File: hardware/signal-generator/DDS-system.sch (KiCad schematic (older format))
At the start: 17 parts

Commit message: [Signal Generator] Layout microcontroller and allocate its pins
The microcontroller is the brains of the function generator system - it
is responsible for controlling the DDS signal generator system, as well
as the LCD module which provides the user interface. The specific
microcontroller used in this project is the ATmega2561-16AU from the
megaAVR uC family. The reasons I have picked this particular part are
the following:
- I am familiar with the AVR uC structure;
- it provides more SRAM memory (8 kB) than other MCUs of the same family;
- it has fewer pins (and therefore peripherals) than the ATmega2560.
Only a fraction of the available peripheral pins of the ATmega2561 have
been utilized in the current design. The remaining port pins (which are
internally connected to useful peripherals such as JTAG, XMEM, etc.)
are connected to pin header connectors and are meant for
upgrading/modifying the system as a whole by including additional
external circuitry. The ATmega2561's SPI port is also connected to a
similar pin header connector which allows the uC to play the role of an
SPI slave device.
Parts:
- removed U?: AD9764AR, Housings_SOIC:SOIC-28W_7.5x17.9mm_Pitch1.27mm, symbol TxDAC:AD9764AR
- removed U?: CY7C1021D-10ZSXI, symbol SRAMs:CY7C1021D-10ZSXI
- removed U?: DS1085Z-10+, symbol Frequency_Synthesizers:DS1085Z-10+
- added U?: AD9764AR, Housings_SOIC:SOIC-28W_7.5x17.9mm_Pitch1.27mm, symbol ulib_TxDAC:AD9764AR
- added U?: CY7C1021D-10ZSXI, symbol ulib_SRAMs:CY7C1021D-10ZSXI
- added U?: DS1085Z-10+, symbol ulib_Frequency_Synthesizers:DS1085Z-10+
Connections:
- net labels added: IOExINTA, IOExINTB
- wire segments 175 -> 177
- no-connect marks 2 -> 0
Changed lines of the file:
@@
 $Descr A4 11693 8268
 encoding utf-8
-Sheet 2 4
+Sheet 2 6
 Title "Digital Function Generator v2 - DDS System"
-Date "2019-11-05"
+Date "2019-12-01"
 Rev "1"
 Comp "Petar Nikolov"
@@
 Comment4 ""
 $EndDescr
-$Comp
-L TxDAC:AD9764AR U?
-U 1 1 5DBB83CF
-P 8100 2500
-F 0 "U?" H 7650 1550 50  0000 C CNN
-F 1 "AD9764AR" H 8500 1550 50  0000 C CNN
-F 2 "Housings_SOIC:SOIC-28W_7.5x17.9mm_Pitch1.27mm" H 8100 2450 50  0001 C CNN
-F 3 "https://www.analog.com/media/en/technical-documentation/data-sheets/AD9764.pdf" H 8100 2550 50  0001 C CNN
-	1    8100 2500
-	1    0    0    -1
-$EndComp
-$Comp
-L SRAMs:CY7C1021D-10ZSXI U?
-U 1 1 5DBB84FF
-P 5250 2550
-F 0 "U?" H 4800 3750 50  0000 C CNN
-F 1 "CY7C1021D-10ZSXI" V 5250 2550 50  0000 C CNN
-F 2 "" H 4450 3300 50  0001 C CNN
-F 3 "https://www.cypress.com/file/42721/download" H 5250 2600 50  0001 C CNN
-	1    5250 2550
-	1    0    0    -1
-$EndComp
-$Comp
-L Frequency_Synthesizers:DS1085Z-10+ U?
-U 1 1 5DBB873B
-P 1550 3350
-F 0 "U?" H 1200 3050 50  0000 C CNN
-F 1 "DS1085Z-10+" H 1900 3050 50  0000 C CNN
-F 2 "" H 0   3300 50  0001 C CNN
-F 3 "https://datasheets.maximintegrated.com/en/ds/DS1085.pdf" H 1550 3350 50  0001 C CNN
-	1    1550 3350
-	1    0    0    -1
-$EndComp
 $Comp
 L Interface_Expansion:MCP23017_SO U?
@@
 Wire Wire Line
 	5250 6800 5250 6900
-NoConn ~ 4550 5500
-NoConn ~ 4550 5600
 Wire Wire Line
 	4550 6300 4450 6300
@@
 	1    0    0    -1
 $EndComp
+$Comp
+L ulib_TxDAC:AD9764AR U?
+U 1 1 5DDD4020
+P 8100 2500
+F 0 "U?" H 8550 1550 50  0000 C CNN
+F 1 "AD9764AR" H 7650 1550 50  0000 C CNN
+F 2 "Housings_SOIC:SOIC-28W_7.5x17.9mm_Pitch1.27mm" H 8100 2450 50  0001 C CNN
+F 3 "https://www.analog.com/media/en/technical-documentation/data-sheets/AD9764.pdf" H 8100 2550 50  0001 C CNN
+	1    8100 2500
+	1    0    0    -1
+$EndComp
+$Comp
+L ulib_SRAMs:CY7C1021D-10ZSXI U?
+U 1 1 5DDE4989
+P 5250 2550
+F 0 "U?" H 5800 1350 50  0000 C CNN
+F 1 "CY7C1021D-10ZSXI" V 5250 2600 50  0000 C CNN
+F 2 "" H 4450 3300 50  0001 C CNN
+F 3 "https://www.cypress.com/file/42721/download" H 5250 2600 50  0001 C CNN
+	1    5250 2550
+	1    0    0    -1
+$EndComp
+$Comp
+L ulib_Frequency_Synthesizers:DS1085Z-10+ U?
+U 1 1 5DDE50A7
+P 1550 3350
+F 0 "U?" H 1200 3050 50  0000 C CNN
+F 1 "DS1085Z-10+" H 1900 3050 50  0000 C CNN
+F 2 "" H 0   3300 50  0001 C CNN
+F 3 "https://datasheets.maximintegrated.com/en/ds/DS1085.pdf" H 1550 3350 50  0001 C CNN
+	1    1550 3350
+	1    0    0    -1
+$EndComp
+Wire Wire Line
+	4550 5500 4450 5500
+Wire Wire Line
+	4450 5600 4550 5600
+Text HLabel 4450 5600 0    50   Input ~ 0
+IOExINTA
+Text HLabel 4450 5500 0    50   Input ~ 0
+IOExINTB
 $EndSCHEMATC

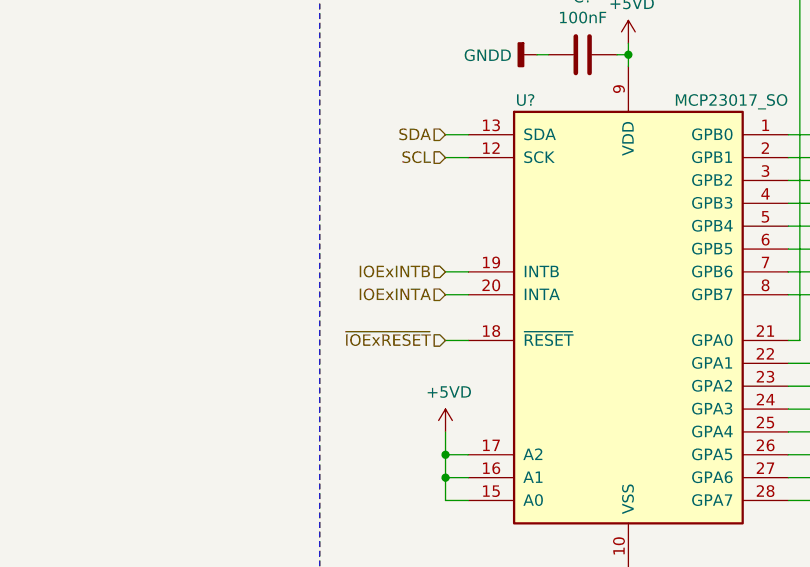
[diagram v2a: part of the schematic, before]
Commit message: [Signal Generator] Add DAC output conversion stage
The additional opamp stage is a differential amplifier configuration
which converts the differential current outputs of the DAC to a singular
voltage output in the range -0.5V to +0.5V.

The electrical schematic has overall been finalized with this addition.
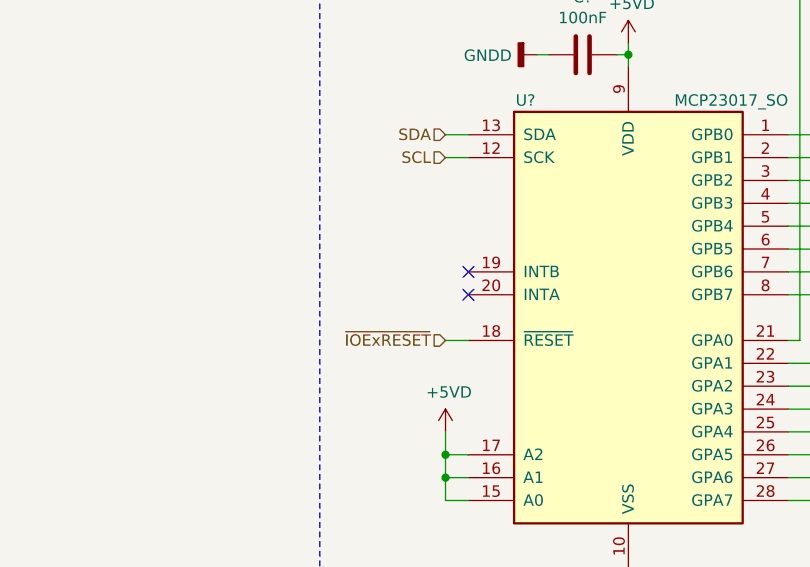
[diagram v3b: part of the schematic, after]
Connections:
- net IOExINTA: no longer names the net of U?.20 (INTA)
- net IOExINTB: no longer names the net of U?.19 (INTB)
- no-connect marks 0 -> 2
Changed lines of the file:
@@
 $Descr A4 11693 8268
 encoding utf-8
-Sheet 2 7
+Sheet 2 6
 Title "Digital Function Generator v2 - DDS System"
-Date "2019-12-01"
+Date "2019-12-08"
 Rev "1"
 Comp "Petar Nikolov"
@@
 	1    0    0    -1
 $EndComp
-Wire Wire Line
-	4550 5500 4450 5500
-Wire Wire Line
-	4450 5600 4550 5600
-Text HLabel 4450 5600 0    50   Input ~ 0
-IOExINTA
-Text HLabel 4450 5500 0    50   Input ~ 0
-IOExINTB
+NoConn ~ 4550 5600
+NoConn ~ 4550 5500
 $EndSCHEMATC

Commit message: [Signal Generator] Implement +3.3VD line with TC1017 voltage regulator
Up until now, the +3.3VD line was implemented using the L78L33 linear
voltage regulator. However, the latter has a dropout voltage of 2V which
means that the L78L33 cannot output a stable +3.3V from a +5V input.

To solve the aforementioned problem the TC1017 LDO voltage regulator has
replaced the L78L33. The former has a low dropout voltage of 180mV (typ.) at
100mA load current.
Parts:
- C? (x9): footprint (none) -> Capacitors_SMD:C_1206_HandSoldering
- C? (x2): footprint (none) -> Capacitors_Tantalum_SMD:CP_Tantalum_Case-A_EIA-3216-18_Hand
- R?: footprint (none) -> Resistors_SMD:R_1206_HandSoldering
- U?: footprint Package_SO:SOIC-28W_7.5x17.9mm_P1.27mm -> Housings_SOIC:SOIC-28W_7.5x17.9mm_Pitch1.27mm
- U?: footprint (none) -> Housings_SOIC:SOIC-14_3.9x8.7mm_Pitch1.27mm
- U?: footprint (none) -> SOP80P1176X120-44N:SOP80P1176X120-44N
- U?: footprint (none) -> Housings_SOIC:SOIC-8_3.9x4.9mm_Pitch1.27mm

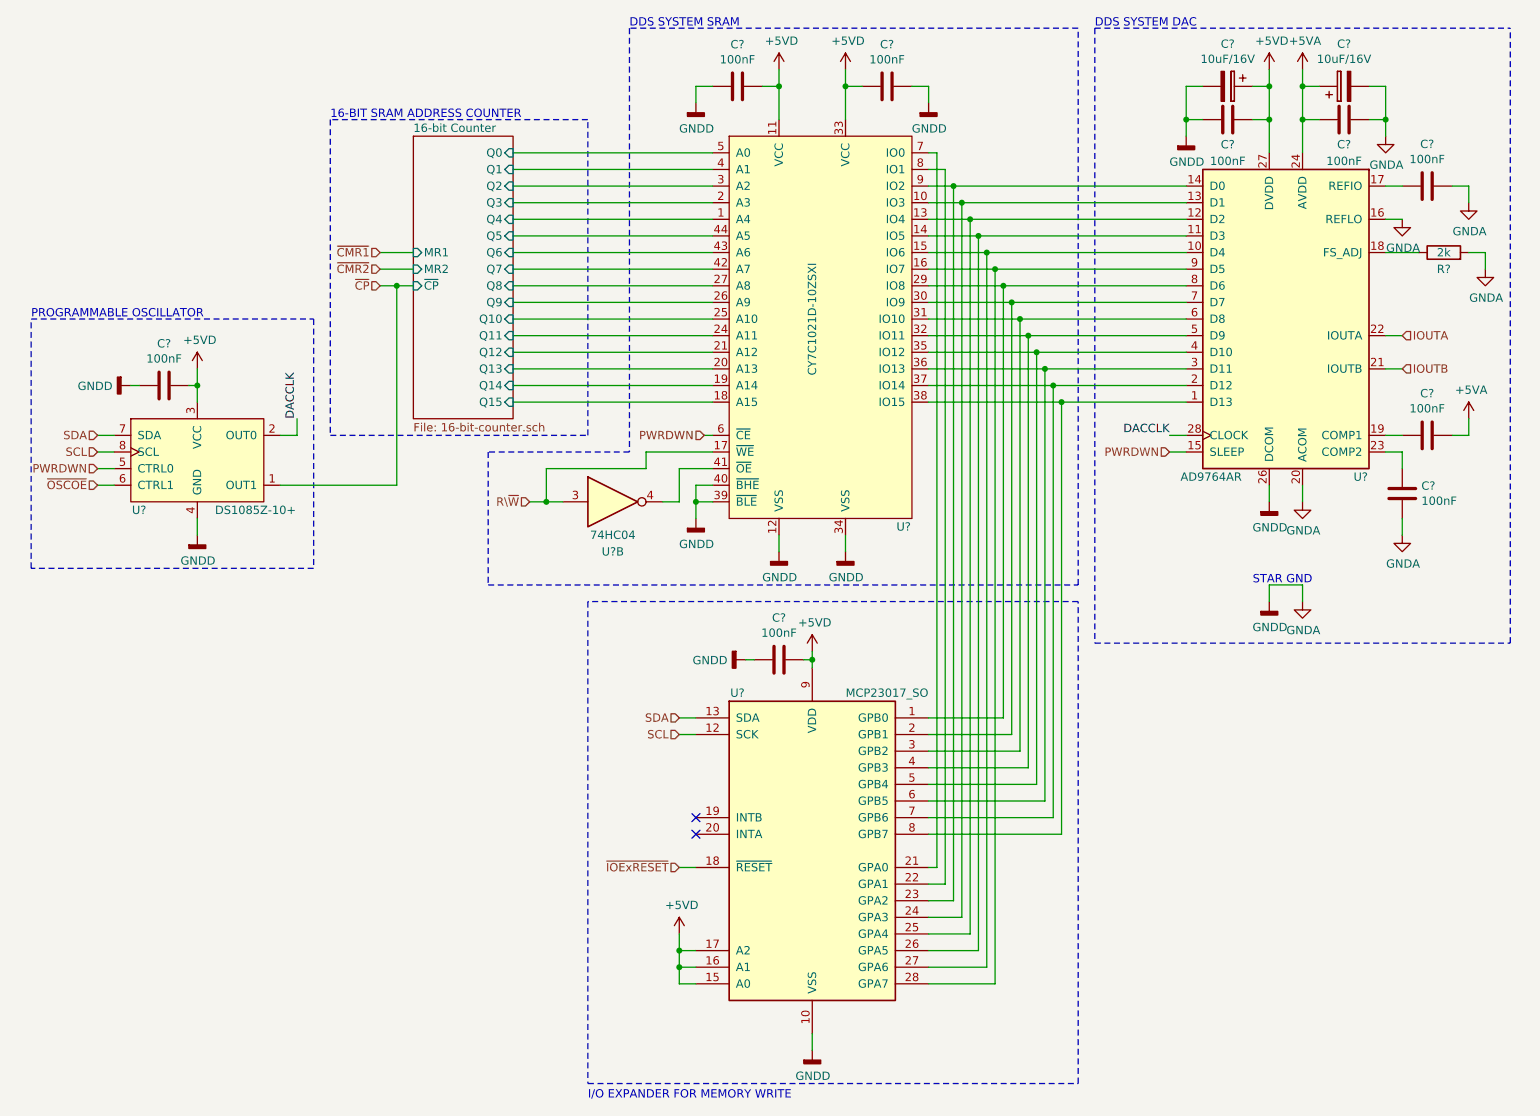
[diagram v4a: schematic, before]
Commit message: [Signal Generator] Use external reference for DAC. Change MCP23017's I2C address
The DDS system's DAC (AD9764 or any other from the TxDAC family)
previously was set up to use its internal 1.2V reference. However, due
to production tolerances, this reference is quite inaccurate ranging
from 1.08V to 1.32V (taken from the AD9764's datasheet). Since this
inaccuracy would greatly affect the generator's precision, I have
decided to use an external voltage reference. Said reference is
generated by the TC4061A which produces a very accurate (0.1% deviation)
1.25V reference.

Also, the I/O expander's (MCP23017's) I2C address has been changed from
'0100 111' to '0100 000'.
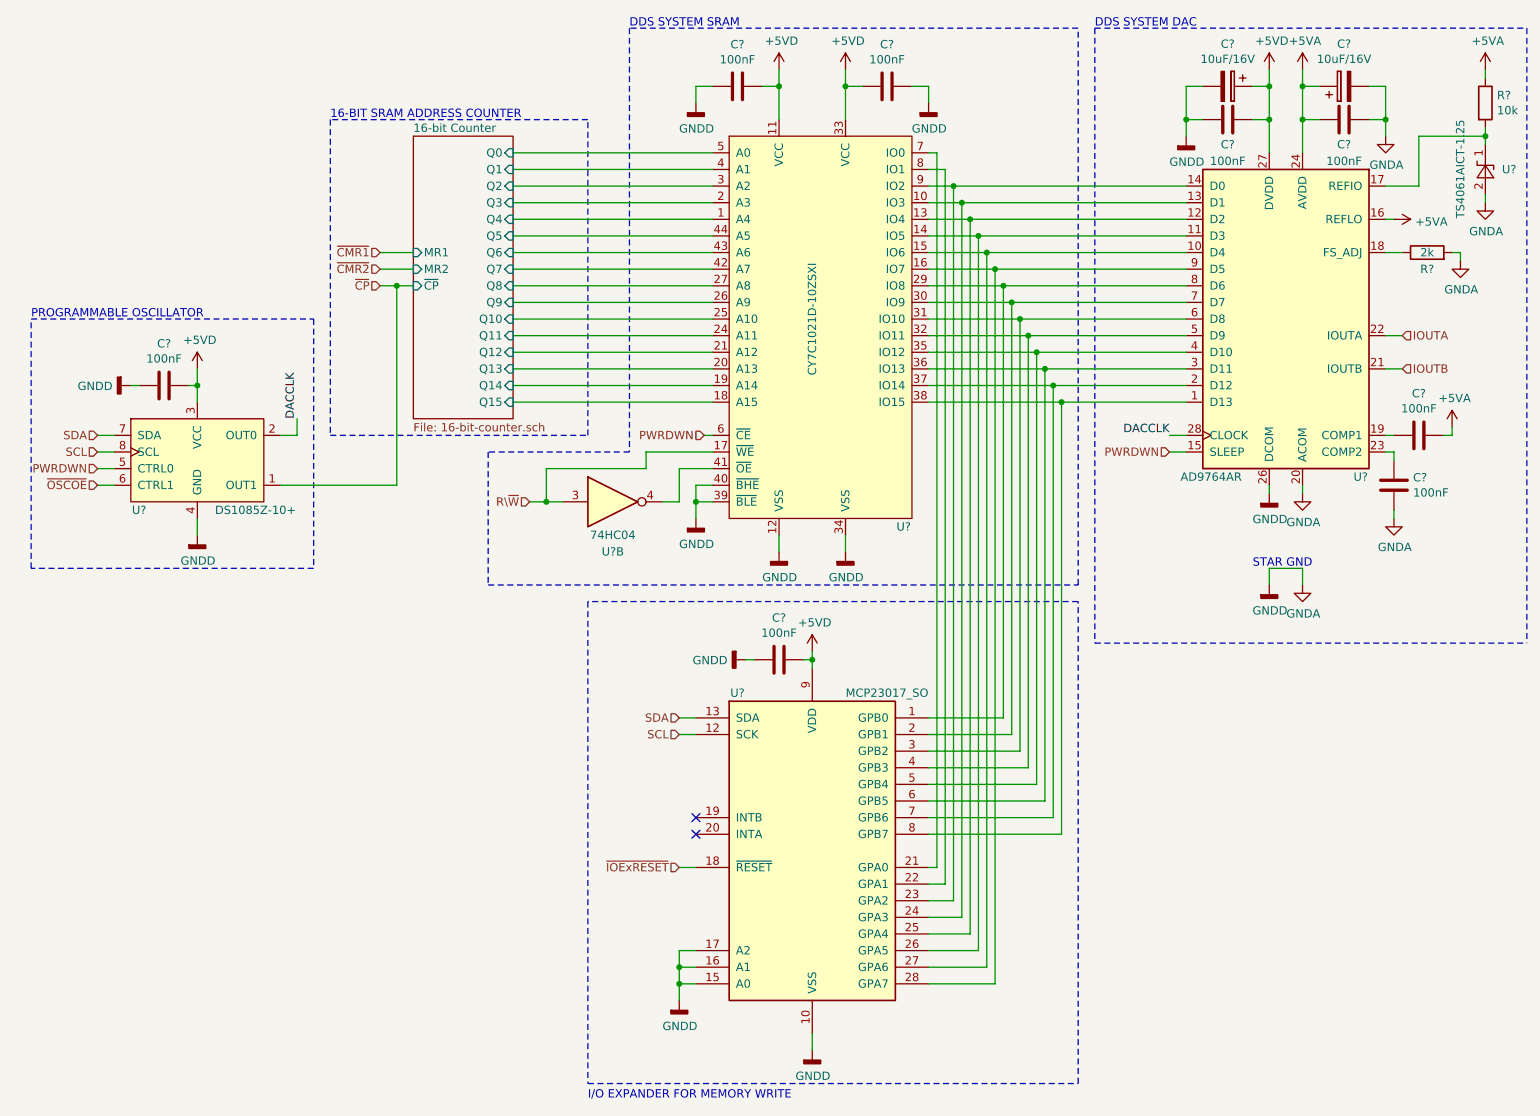
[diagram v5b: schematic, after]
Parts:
- removed C?: 100nF, Capacitors_SMD:C_1206_HandSoldering, symbol Device:C
- added R?: 10k, symbol Device:R
- added U?: TS4061AICT-1.25, symbol ulib_Voltage_References:TS4061xIxT-1.25
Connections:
- net +5VA: now also U?.16 (REFLO), R?.1
- net +5VD: no longer U?.15 (A0), U?.16 (A1), U?.17 (A2)
- net GNDA: now also U?.15 (A0), U?.16 (A1), U?.17 (A2), U?.2 (A); no longer U?.16 (REFLO)
- net at U?.17 (REFIO): now also R?.2, U?.1 (K)
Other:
- moved on the sheet: C?, R?
